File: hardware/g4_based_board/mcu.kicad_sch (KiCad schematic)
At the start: 17 parts, among them SW1 RESET, SW2 SW_SPDT, U1 STM32G431R6Tx, Y1 12MHz, 20pF

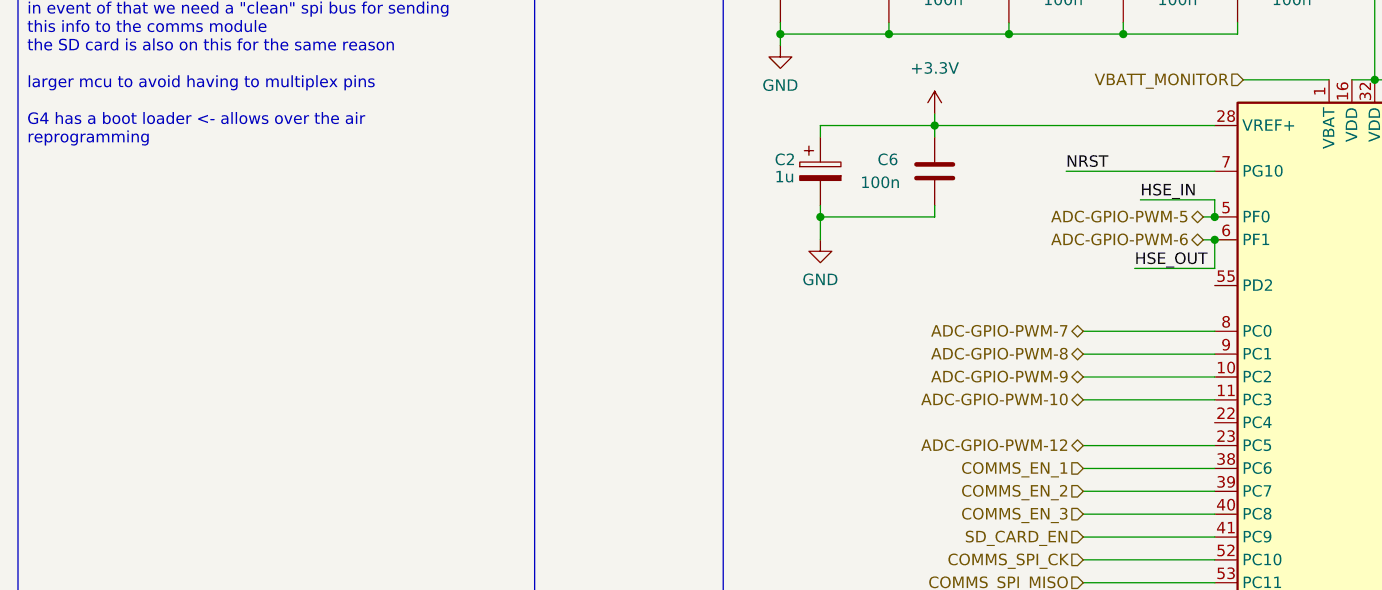
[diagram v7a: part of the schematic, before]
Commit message: updated .ioc to reflect changes make in pcb
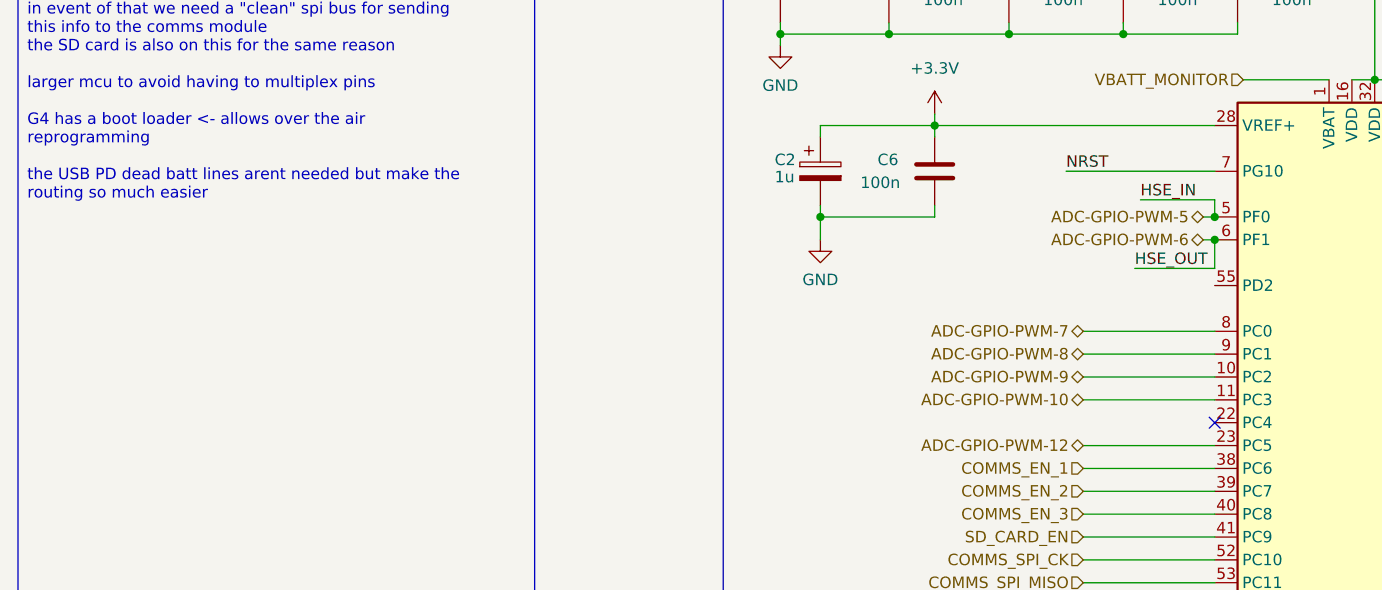
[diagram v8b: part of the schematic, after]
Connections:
- no-connect marks 1 -> 2
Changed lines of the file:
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@@
 		(at 103.505 69.215)
+	)
+	(no_connect
+		(at 67.945 81.915)
 	)
 	(wire
@@
 		)
 	)
-	(text_box "there are 2 SPI buses one for the digital out sensors and one for comms\nthis was done because its more likely one of the comms sensors will go dark and fuck up the bus, and in event of that we need a \"clean\" spi bus for sending this info to the comms module\nthe SD card is also on this for the same reason\n\nlarger mcu to avoid having to multiplex pins\n\nG4 has a boot loader <- allows over the air reprogramming"
+	(text_box "there are 2 SPI buses one for the digital out sensors and one for comms\nthis was done because its more likely one of the comms sensors will go dark and fuck up the bus, and in event of that we need a \"clean\" spi bus for sending this info to the comms module\nthe SD card is also on this for the same reason\n\nlarger mcu to avoid having to multiplex pins\n\nG4 has a boot loader <- allows over the air reprogramming\n\nthe USB PD dead batt lines arent needed but make the routing so much easier"
 		(exclude_from_sim no)
 		(at -65.024 25.908 0)
